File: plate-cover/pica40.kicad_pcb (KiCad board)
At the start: 2 copper layers, 134.3 x 93.7 mm, 27 parts, among them SW1 SW_PUSH, SW10 SW_PUSH, SW11 SW_PUSH, SW12 SW_PUSH, SW13 SW_PUSH, SW14 SW_PUSH, SW15 SW_PUSH, SW16 SW_PUSH, SW17 SW_PUSH, SW18 SW_PUSH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

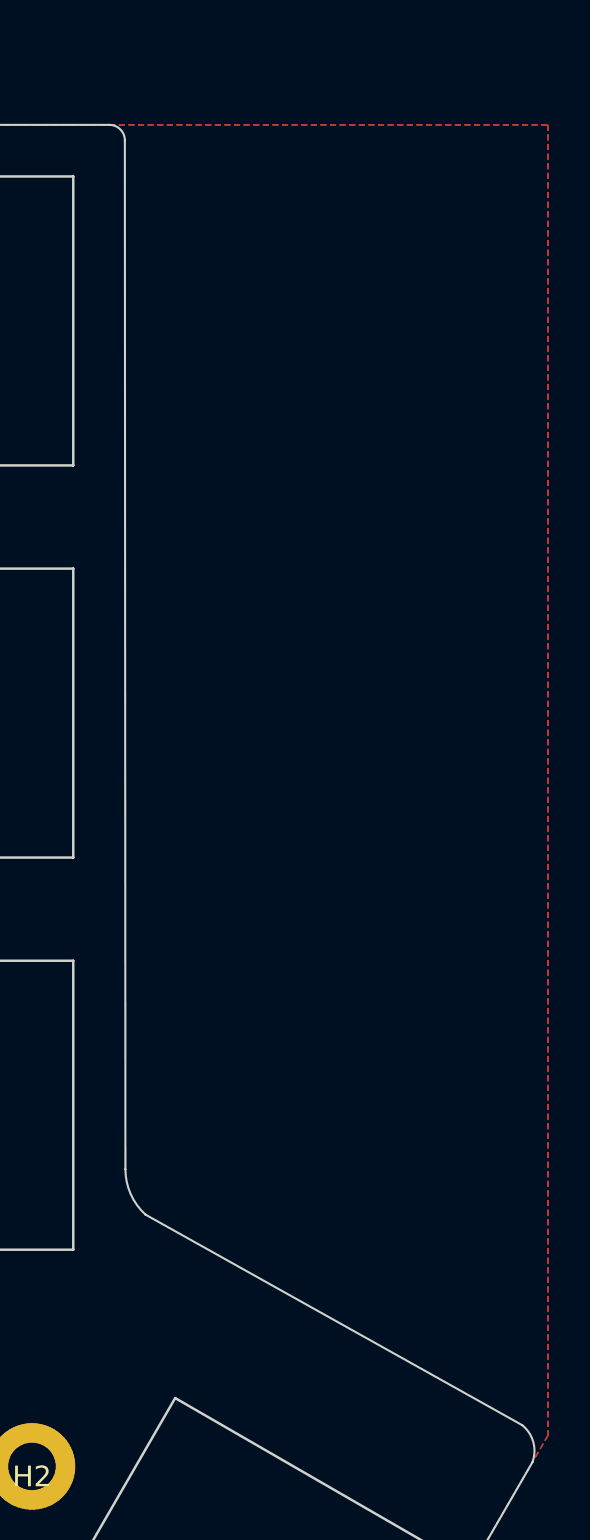
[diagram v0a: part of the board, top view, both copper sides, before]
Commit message: add breakaway plate, replace battery connector
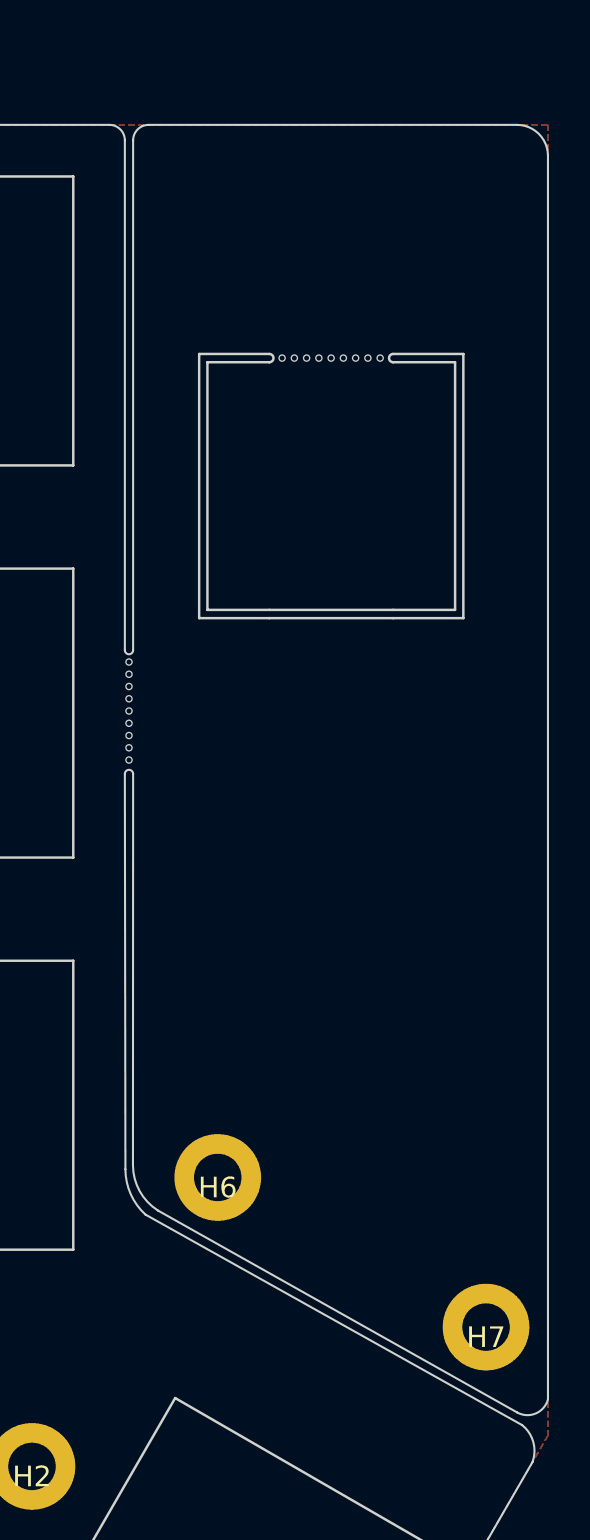
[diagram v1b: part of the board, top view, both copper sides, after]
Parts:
- added BR1: MountingHole, kbd:Breakaway_Tabs, F.Cu at (183.2, 86.4)
- added H6: MountingHole, kbd:M2_Hole_TH, F.Cu at (187.5, 109.0)
- added H7: MountingHole, kbd:M2_Hole_TH, F.Cu at (200.5, 116.2)
- added RE1: RotaryEncoder_Switch, pica:EC11_Hole_Breakaway, F.Cu at (193.0, 75.5)
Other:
- board size 134.3 x 93.7 mm -> 135 x 93.7 mm
